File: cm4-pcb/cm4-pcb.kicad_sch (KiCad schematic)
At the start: 6 parts, among them U1 Pfostenstecker_6_2x3

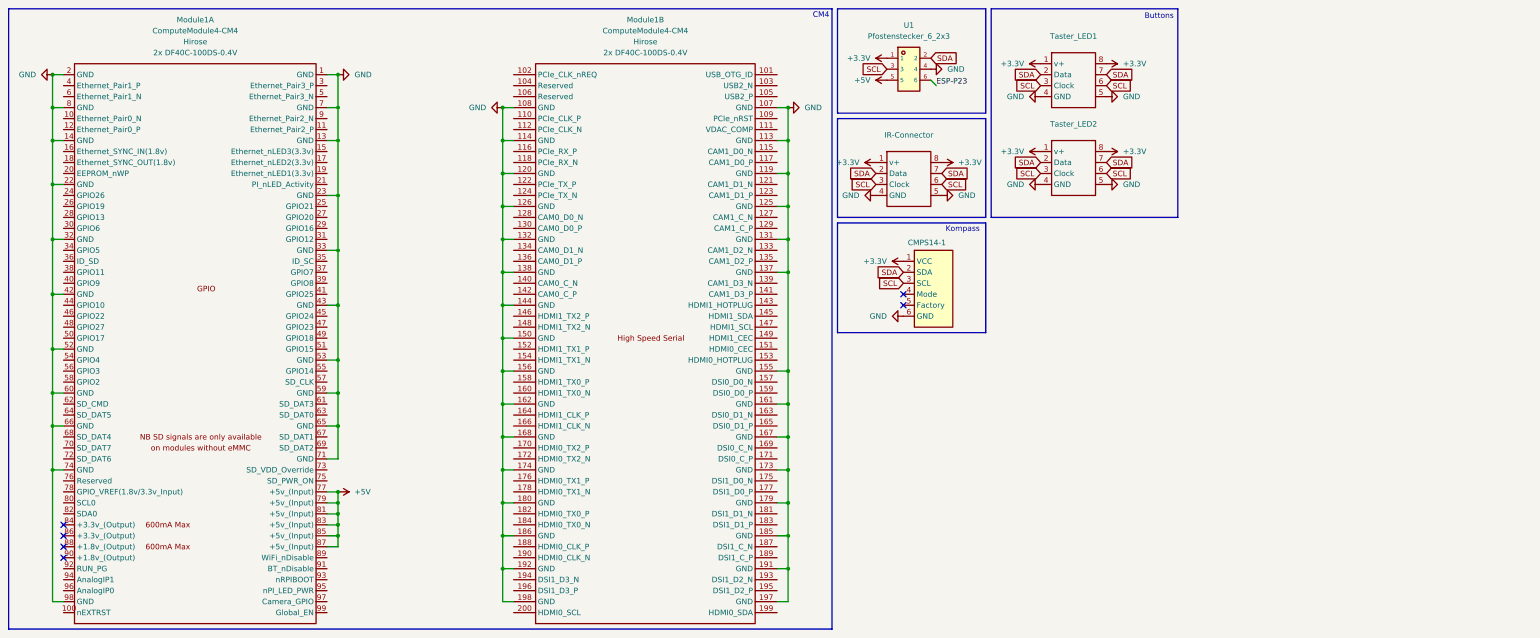
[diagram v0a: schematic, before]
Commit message: rerouted gnd and added NC flag
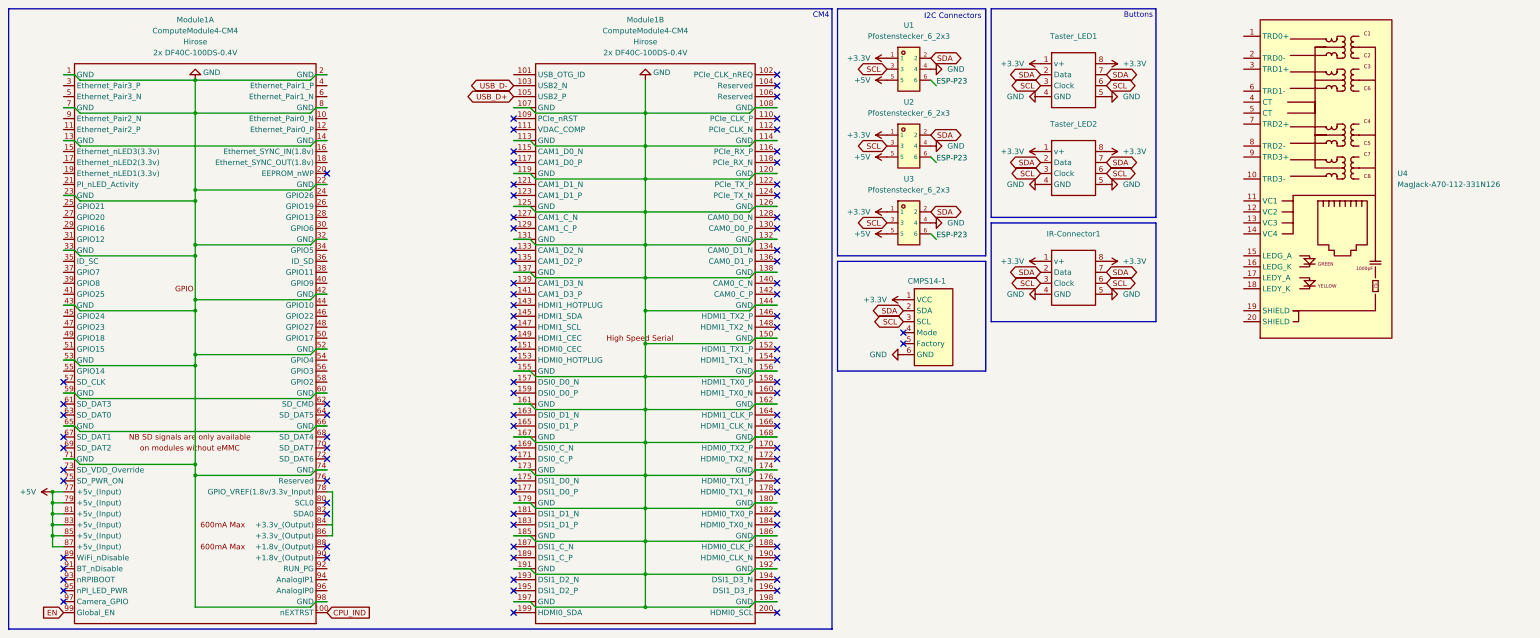
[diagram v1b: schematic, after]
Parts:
- added U2, U3: Pfostenstecker_6_2x3, BohleBots:HDR-TH_6P-P2.54-V-F-R2-C3-S2.54-4, symbol bohlebots.lib:Pfostenstecker_6_2x3
- added U4: MagJack-A70-112-331N126, CM4IO:TRJG0926HENL, symbol CM4IO:MagJack-A70-112-331N126
- CMPS14-1: footprint (none) -> sarcat:CMPS14
- renumbered IR-Connector to IR-Connector1
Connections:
- net +3.3V: now also U2.1, U3.1
- net +5V: now also U2.5, U3.5
- net ESP-P23: now also U2.6, U3.6
- net GND: now also U2.4, U3.4; no longer Module1.13 (GND), Module1.14 (GND), Module1.59 (GND), Module1.60 (GND), Module1.65 (GND), Module1.66 (GND)
- net SCL: now also U2.3, U3.3
- net SDA: now also U2.2, U3.2
- net CPU_IND: now reaches Module1.100 (nEXTRST)
- net at Module1.78 (GPIO_VREF(1.8v/3.3v_Input)): now also Module1.86 (+3.3v_(Output))
- net EN: now reaches Module1.99 (Global_EN)
- net USB_D-: now reaches Module1.103 (USB2_N)
- net USB_D+: now reaches Module1.105 (USB2_P)
- new net: Module1.13 (GND), Module1.14 (GND)
- new net: Module1.59 (GND), Module1.60 (GND)
- new net: Module1.65 (GND), Module1.66 (GND)
- no-connect marks 6 -> 92
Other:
- note added: "I2C Connectors"
- note removed: "Kompass"
- moved on the sheet: CMPS14-1, IR-Connector1, Module1A

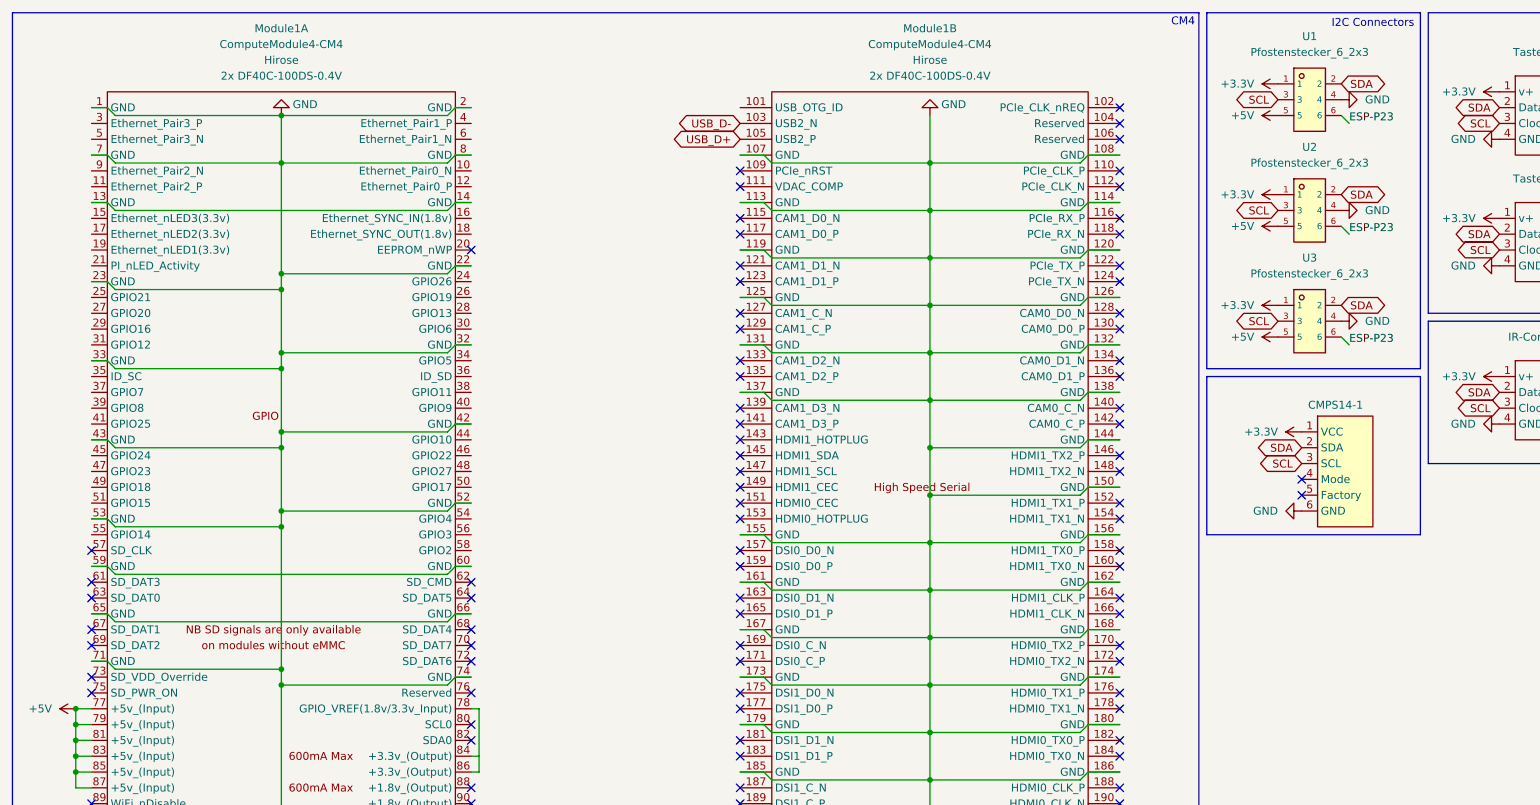
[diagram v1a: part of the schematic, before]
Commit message: Added additional I2C Pullup resistor
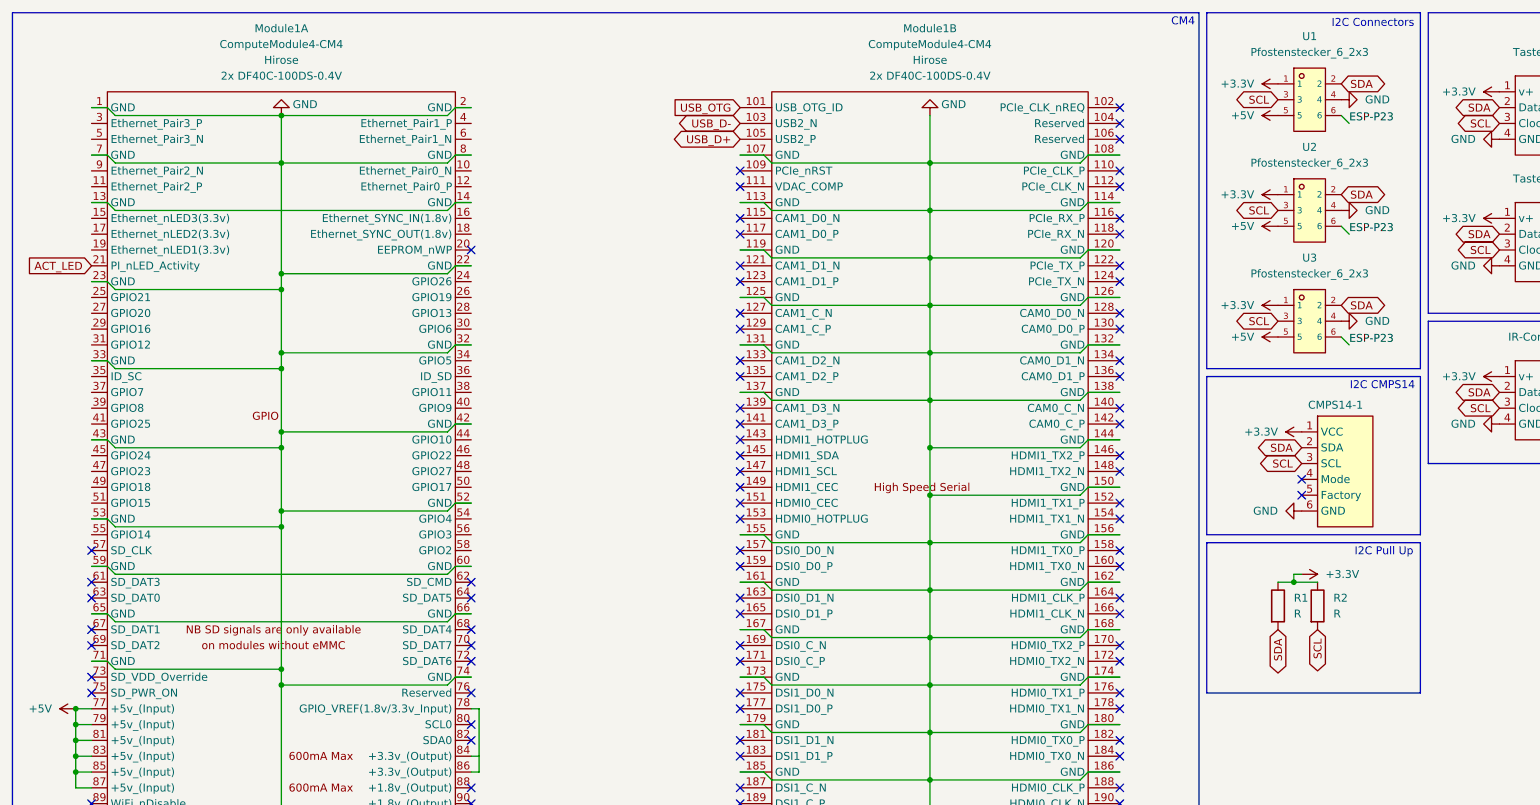
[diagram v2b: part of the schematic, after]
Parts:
- added R1, R2: R, BohleBots:R_THT, symbol Device:R
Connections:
- net +3.3V: now also R1.1, R2.1
- net SCL: now also R2.2
- net SDA: now also R1.2
- net ACT_LED: now reaches Module1.21 (PI_nLED_Activity)
- net USB_OTG: now reaches Module1.101 (USB_OTG_ID)
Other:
- note added: "I2C CMPS14"
- note added: "I2C Pull Up"

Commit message: Shutdown button
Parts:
- added R3: SMD-10k, BohleBots:R0603, symbol bohlebots.lib:SMD-10k
- added U5: SMD-PUSH-BTN, BohleBots:SW-TH_5P-L6.0-W6.0-P4.50-LS6.5, symbol bohlebots.lib:SMD-PUSH-BTN
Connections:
- net USB_OTG is gone; now on net GND: Module1.101 (USB_OTG_ID)
- net +3.3V: now also R3.2
- net GND: now also U5.3, U5.4, U5.5
- net RESET: now reaches Module1.92 (RUN_PG)
- new net SHUTDOWN: R3.1, U5.1, U5.2
- no-connect marks 92 -> 94
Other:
- note added: "Grounded for fixed use as USB Host, datasheet chapter 2.4 and pinout"
- note added: "Shutdown Button"

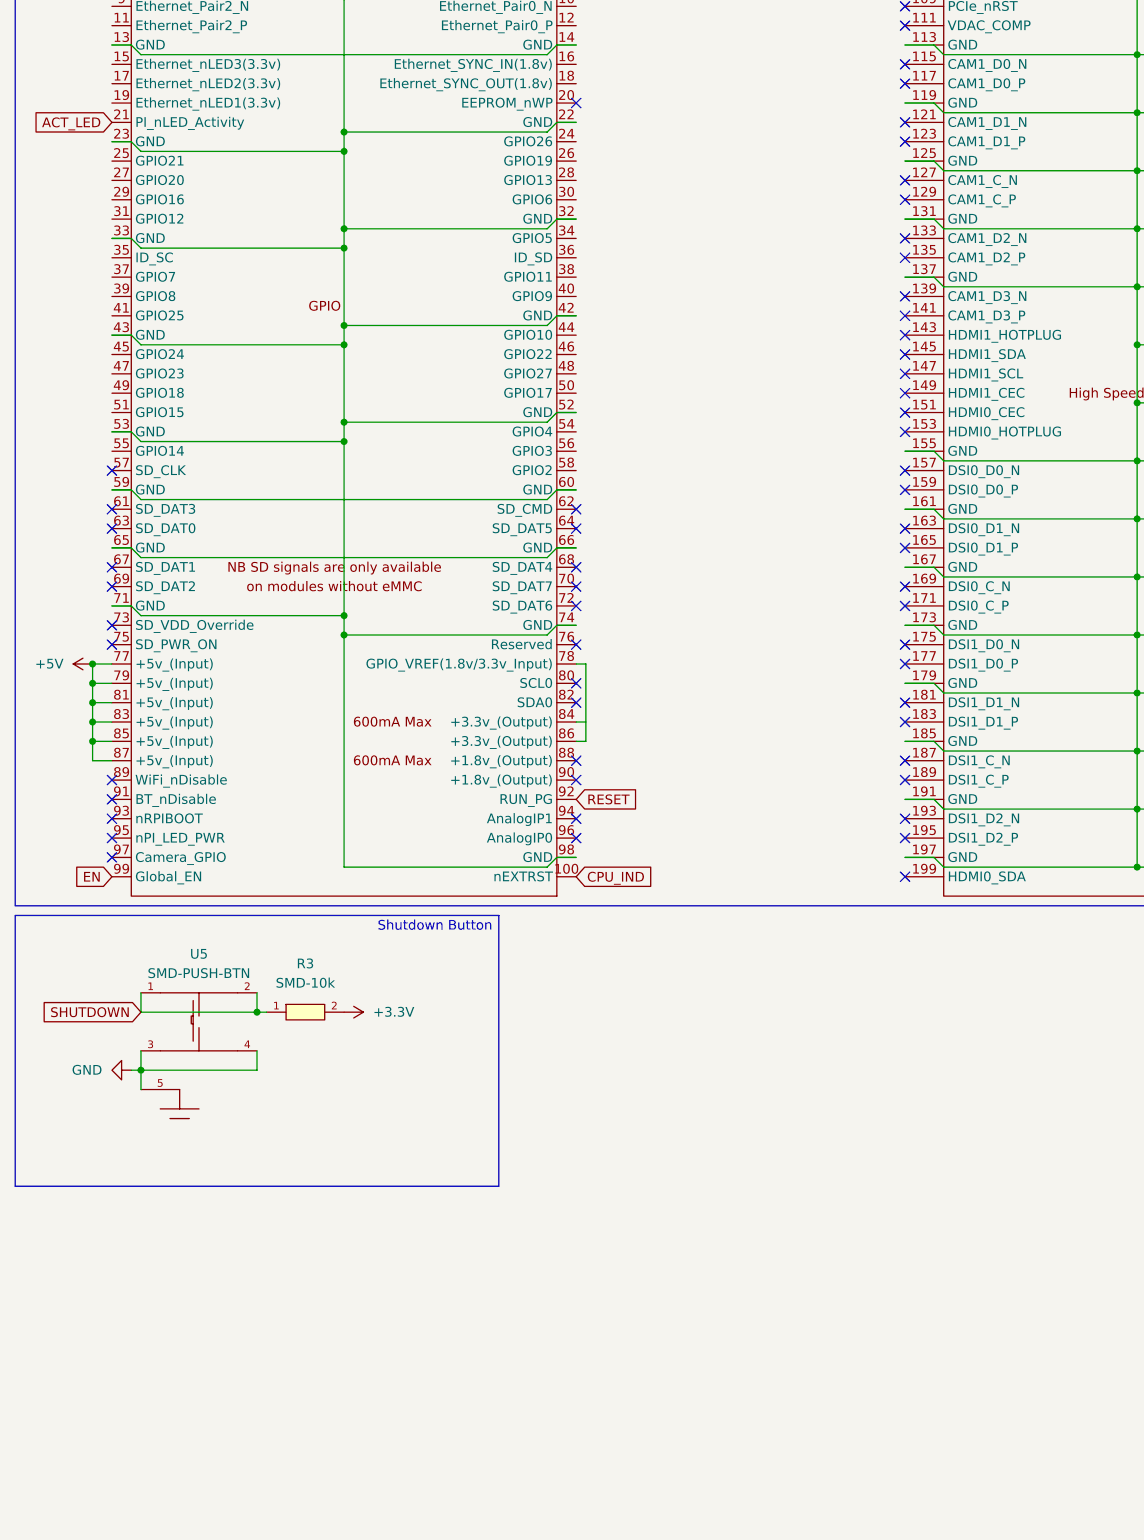
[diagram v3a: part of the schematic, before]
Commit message: Activity LED + Reset Pins + GPIO Pins
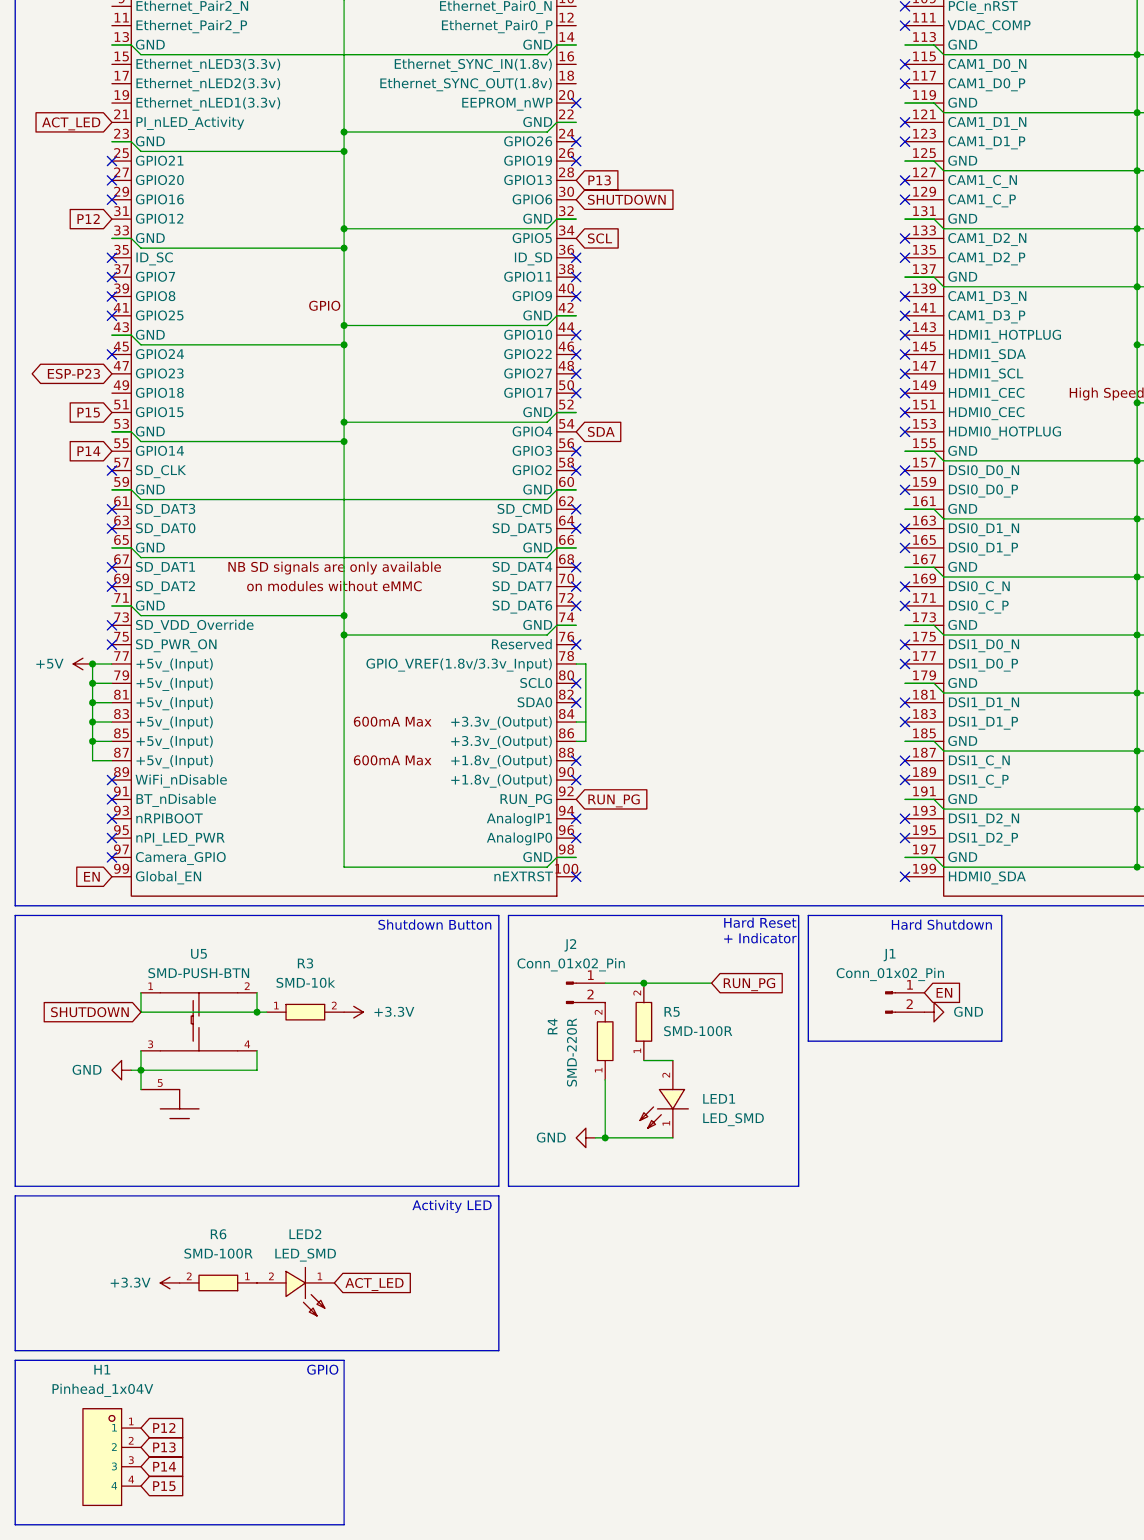
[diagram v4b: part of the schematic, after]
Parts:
- added H1: Pinhead_1x04V, BohleBots:HDR-TH_4P-P2.54-V-M-1, symbol bohlebots.lib:Pinhead_1x04V
- added J1, J2: Conn_01x02_Pin, Connector_PinHeader_2.54mm:PinHeader_1x02_P2.54mm_Vertical, symbol Connector:Conn_01x02_Pin
- added LED1, LED2: LED_SMD, BohleBots:LED-SMD_L1.7-W0.6-RD, symbol bohlebots.lib:LED_SMD
- added R4: SMD-220R, BohleBots:R0603, symbol bohlebots.lib:SMD-220R
- added R5, R6: SMD-100R, BohleBots:R0603, symbol bohlebots.lib:SMD-100R
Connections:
- net +3.3V: now also R6.2
- net ACT_LED: now also LED2.1 (K)
- net EN: now also J1.1 (Pin_1)
- net ESP-P23: now also Module1.47 (GPIO23)
- net GND: now also J1.2 (Pin_2), LED1.1 (K), R4.1
- net SCL: now also Module1.34 (GPIO5)
- net SDA: now also Module1.54 (GPIO4)
- net SHUTDOWN: now also Module1.30 (GPIO6)
- net P13: now reaches Module1.28 (GPIO13)
- net P13: now also H1.2
- net P12: now reaches Module1.31 (GPIO12)
- net P12: now also H1.1
- net P15: now reaches Module1.51 (GPIO15)
- net P15: now also H1.4
- net P14: now reaches Module1.55 (GPIO14)
- net P14: now also H1.3
- net CPU_IND: no longer names the net of Module1.100 (nEXTRST)
- net RESET renamed RUN_PG
- net RUN_PG: now also J2.1 (Pin_1), R5.2
- new net: LED1.2 (A), R5.1
- new net: J2.2 (Pin_2), R4.2
- new net: LED2.2 (A), R6.1
- no-connect marks 94 -> 114
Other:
- note added: "Activity LED"
- note added: "GPIO"
- note added: "Hard Reset + Indicator"
- note added: "Hard Shutdown"

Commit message: Ethernet
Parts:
- added C1: SMD-100nF, BohleBots:C0603, symbol bohlebots.lib:SMD-100nF
- added H2: Pinhead_1x04V, BohleBots:HDR-TH_4P-P2.54-V-M-1, symbol bohlebots.lib:Pinhead_1x04V
- added R7, R8: SMD-470R, BohleBots:R0603, symbol bohlebots.lib:SMD-470R
- U4: Field6 (none) -> TRJG0926HENL; Field7 (none) -> Trxcon; Field8 (none) -> UCON00900; Part Description (none) -> Gigabit Ethernet Magjack
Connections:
- net +3.3V: now also U4.15 (LEDG_A), U4.17 (LEDY_A)
- net GND: now also U4.19 (SHIELD), U4.20 (SHIELD), C1.1
- net TRD0_P: now reaches U4.1 (TRD0+)
- net TRD0_P: now also Module1.12 (Ethernet_Pair0_P)
- net TRD3_N: now reaches U4.10 (TRD3-)
- net TRD3_N: now also Module1.5 (Ethernet_Pair3_N)
- net TR0_TAP: now reaches U4.11 (VC1)
- net TR0_TAP: now also H2.1
- net TR1_TAP: now reaches U4.12 (VC2)
- net TR1_TAP: now also H2.2
- net TR2_TAP: now reaches U4.13 (VC3)
- net TR2_TAP: now also H2.3
- net TR3_TAP: now reaches U4.14 (VC4)
- net TR3_TAP: now also H2.4
- net at U4.16 (LEDG_K): now also R7.2
- net at U4.18 (LEDY_K): now also R8.2
- net TRD0_N: now reaches U4.2 (TRD0-)
- net TRD0_N: now also Module1.10 (Ethernet_Pair0_N)
- net TRD1_P: now reaches U4.3 (TRD1+)
- net TRD1_P: now also Module1.4 (Ethernet_Pair1_P)
- net at U4.4 (CT): now also U4.5 (CT), C1.2
- net TRD1_N: now reaches U4.6 (TRD1-)
- net TRD1_N: now also Module1.6 (Ethernet_Pair1_N)
- net TRD2_P: now reaches U4.7 (TRD2+)
- net TRD2_P: now also Module1.11 (Ethernet_Pair2_P)
- net TRD2_N: now reaches U4.8 (TRD2-)
- net TRD2_N: now also Module1.9 (Ethernet_Pair2_N)
- net TRD3_P: now reaches U4.9 (TRD3+)
- net TRD3_P: now also Module1.3 (Ethernet_Pair3_P)
- net ETH_LEDY: now reaches Module1.15 (Ethernet_nLED3(3.3v))
- net ETH_LEDY: now also R8.1
- net ETH_LEDG: now reaches Module1.17 (Ethernet_nLED2(3.3v))
- net ETH_LEDG: now also R7.1
- no-connect marks 114 -> 116
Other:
- note added: "Ethernet"
- note added: "Ethernet Tap"
